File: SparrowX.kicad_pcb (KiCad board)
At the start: 4 copper layers, 31.6 x 26.6 mm, 25 parts, among them J1 NORTH, J2 SOUTH, J3 WEST, J4 EAST, U1 TPS629210-Q1, U2 LD49100PU33RY, U3 STM32G0B1CBU6, U4 TCAN332G, U5 TCAN332G

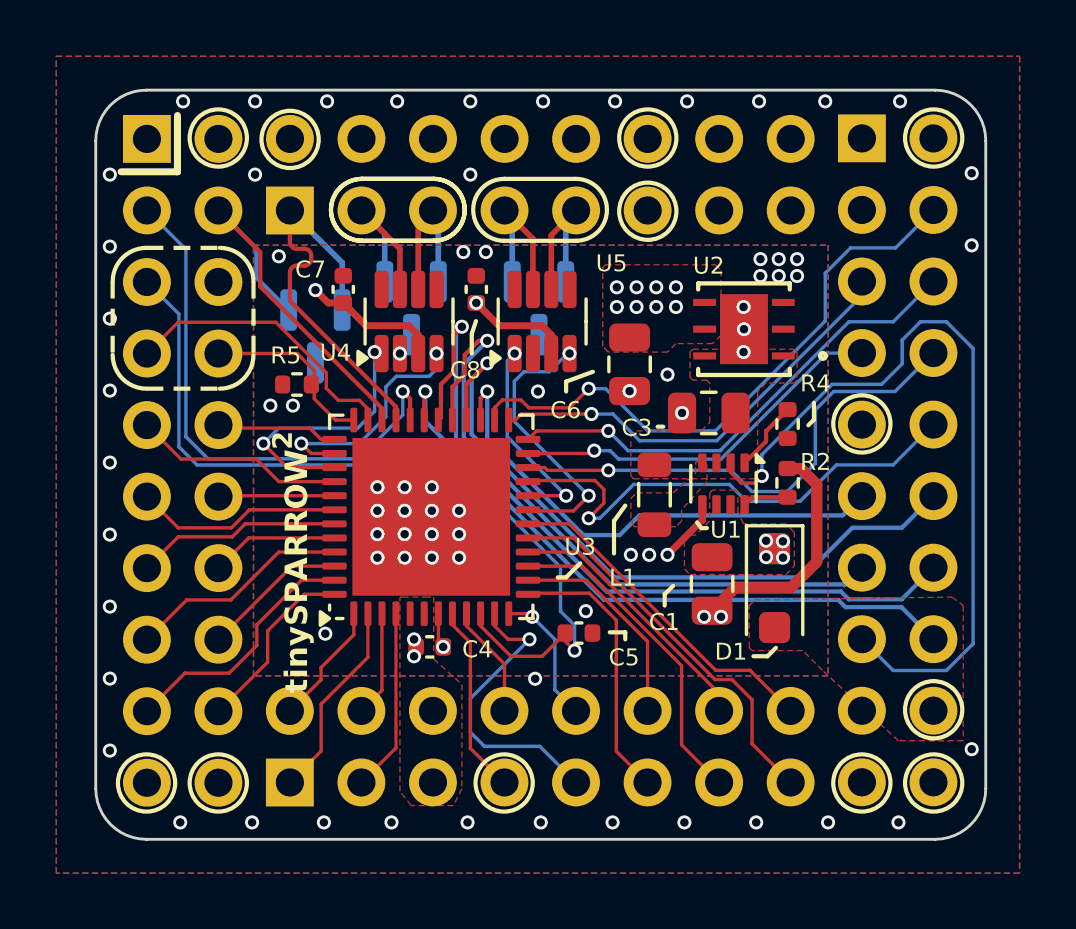
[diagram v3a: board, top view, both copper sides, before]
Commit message: Nudge U2/C3 up a bit to make 3V3 zone wider
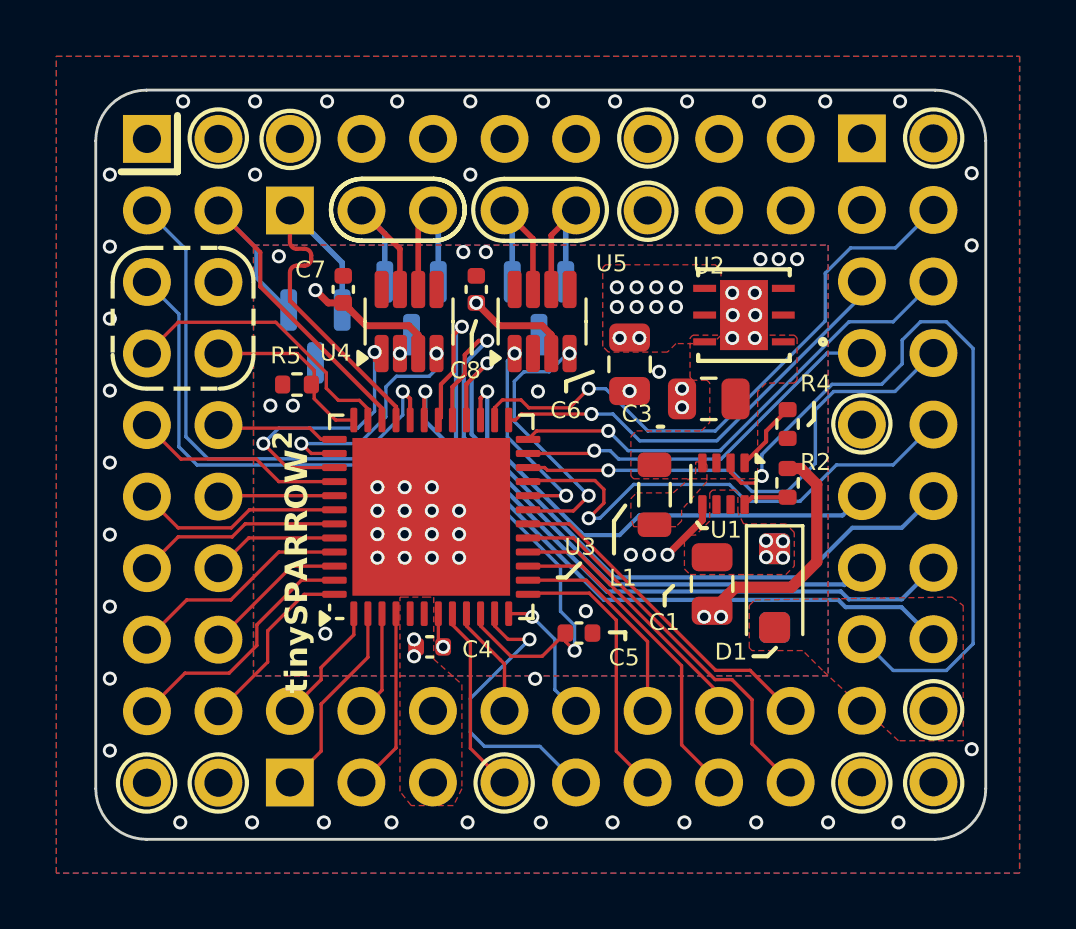
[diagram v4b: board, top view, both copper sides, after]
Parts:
- moved C3 0.50 mm to (176.4, 91.8)
- moved U2 0.50 mm to (177.6, 88.8)
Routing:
- net GND: vias 79 -> 80
- net +3V3: vias 12 -> 14
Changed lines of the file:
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@@
 	(footprint "Capacitor_SMD:C_0805_2012Metric"
 		(layer "F.Cu")
-		(at 176.3652 92.262801 180)
+		(at 176.3652 91.762801 180)
 		(descr "Capacitor SMD 0805 (2012 Metric), square (rectangular) end terminal, IPC_7351 nominal, (Body size source: IPC-SM-782 page 76, https://www.pcb-3d.com/wordpress/wp-content/uploads/ipc-sm-782a_amendment_1_and_2.pdf, https://docs.google.com/spreadsheets/d/1BsfQQcO9C6DZCsRaXUlFlo91Tg2WpOkGARC1WS5S8t0/edit?usp=sharing), generated with kicad-footprint-generator")
 		(tags "capacitor")
@@
 	(footprint "footprint:DFN6_LD49100_STM"
 		(layer "F.Cu")
-		(at 177.6152 89.287799 180)
+		(at 177.6152 88.787799 180)
 		(tags "LD49100PU33RY ")
 		(property "Reference" "U2"
@@
 	)
 	(via
-		(at 177.6 88.5)
+		(at 177.2 88)
 		(size 0.5)
 		(drill 0.3)
@@
 	)
 	(via
-		(at 178.2 87.4)
-		(size 0.5)
-		(drill 0.3)
-		(layers "F.Cu" "B.Cu")
-		(free yes)
-		(net 1)
-	)
-	(via
 		(at 170.481251 81.2)
 		(size 0.5)
@@
 	)
 	(via
-		(at 174.9 90.9)
+		(at 174.6 90.8)
 		(size 0.5)
 		(drill 0.3)
@@
 	)
 	(via
+		(at 178 89.6)
+		(size 0.5)
+		(drill 0.3)
+		(layers "F.Cu" "B.Cu")
+		(net 1)
+	)
+	(via
 		(at 176.2 99.5)
 		(size 0.5)
@@
 	)
 	(via
+		(at 178 88)
+		(size 0.5)
+		(drill 0.3)
+		(layers "F.Cu" "B.Cu")
+		(net 1)
+	)
+	(via
 		(at 155.1 99.1375)
 		(size 0.5)
@@
 	)
 	(via
+		(at 178.0152 88.787799)
+		(size 0.5)
+		(drill 0.3)
+		(layers "F.Cu" "B.Cu")
+		(net 1)
+	)
+	(via
 		(at 167.9 83.8)
 		(size 0.5)
@@
 	)
 	(via
-		(at 179.5 87.4)
+		(at 175.415201 91.4)
 		(size 0.5)
 		(drill 0.3)
 		(layers "F.Cu" "B.Cu")
-		(free yes)
 		(net 1)
 	)
 	(via
-		(at 177.6 90.1)
+		(at 177.2 89.6)
 		(size 0.5)
 		(drill 0.3)
@@
 	)
 	(via
-		(at 175.415201 92.262801)
+		(at 175.415201 92.062801)
 		(size 0.5)
 		(drill 0.3)
@@
 	)
 	(via
-		(at 178.85 87.4)
-		(size 0.5)
-		(drill 0.3)
-		(layers "F.Cu" "B.Cu")
-		(free yes)
-		(net 1)
-	)
-	(via
 		(at 164.6 97.4)
 		(size 0.5)
@@
 	)
 	(via
-		(at 177.6152 89.287799)
+		(at 177.2152 88.787799)
 		(size 0.5)
 		(drill 0.3)
@@
 	)
 	(via
+		(at 173.9 89.6)
+		(size 0.5)
+		(drill 0.3)
+		(layers "F.Cu" "B.Cu")
+		(free yes)
+		(net 2)
+	)
+	(via
 		(at 174.5 88.5)
 		(size 0.5)
@@
 	)
 	(via
+		(at 173.2 89.6)
+		(size 0.5)
+		(drill 0.3)
+		(layers "F.Cu" "B.Cu")
+		(free yes)
+		(net 2)
+	)
+	(via
 		(at 168.110532 88.355201)
 		(size 0.5)
@@
 			(pts
 				(xy 173.6 94.5) (xy 173.6 93.1) (xy 173.8 92.9) (xy 176.1 92.9) (xy 176.4 92.6) (xy 176.4 91.2)
-				(xy 176.3 91.1) (xy 175.8 91.1) (xy 175.7 91) (xy 175.7 90.1) (xy 175.8 90) (xy 179.4 90) (xy 179.5 90.1)
+				(xy 176.3 91.1) (xy 175.8 91.1) (xy 175.7 91) (xy 175.7 89.6) (xy 175.8 89.5) (xy 179.4 89.5) (xy 179.5 89.6)
 				(xy 179.5 91.1) (xy 179.4 91.2) (xy 178.4 91.2) (xy 178.1 91.5) (xy 178.1 94.5) (xy 178 94.6) (xy 173.7 94.6)
 			)
